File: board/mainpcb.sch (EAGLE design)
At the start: 55 parts, among them IC1 ATMEGA328P, IC2 MAX6921, IC3 7805TV, IC4 DS18B20, J1 2.1MMJACK, Q1 32.768 khz, Q2 IRFD110, SW1 OS102011MA1Q

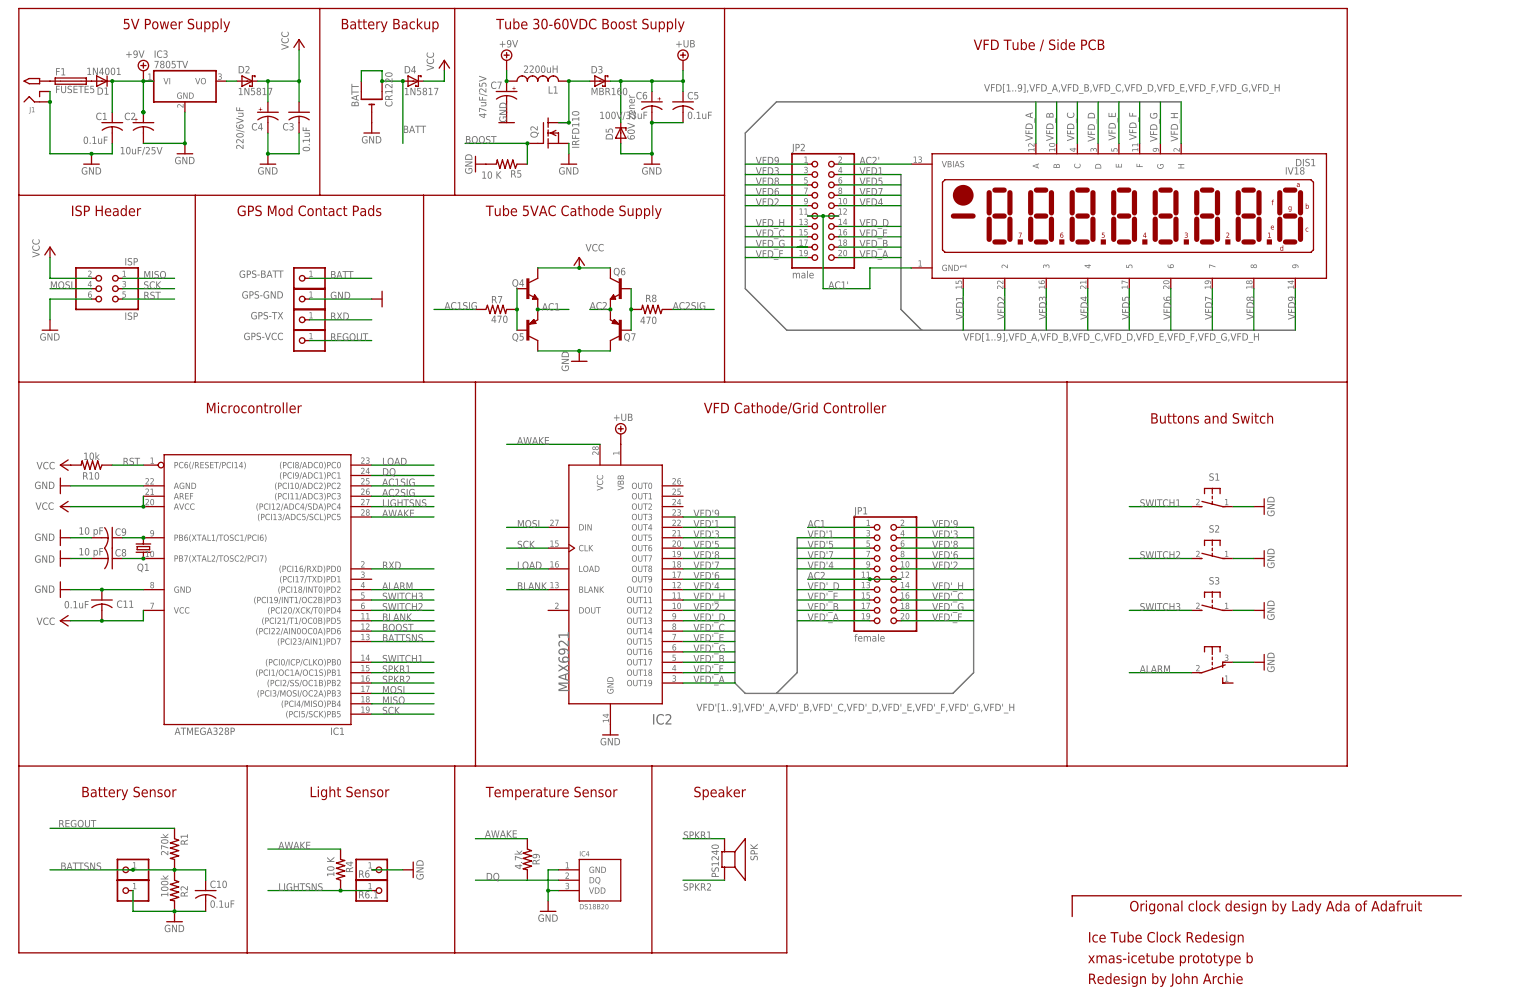
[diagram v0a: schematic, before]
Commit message: Revised the xmas-icetube board
This commit updates the Ice Tube Clock board to revision C.  Although
revision C is untested, the circuit is identical to revision B, so I
cannot imagine that there would be any problems.
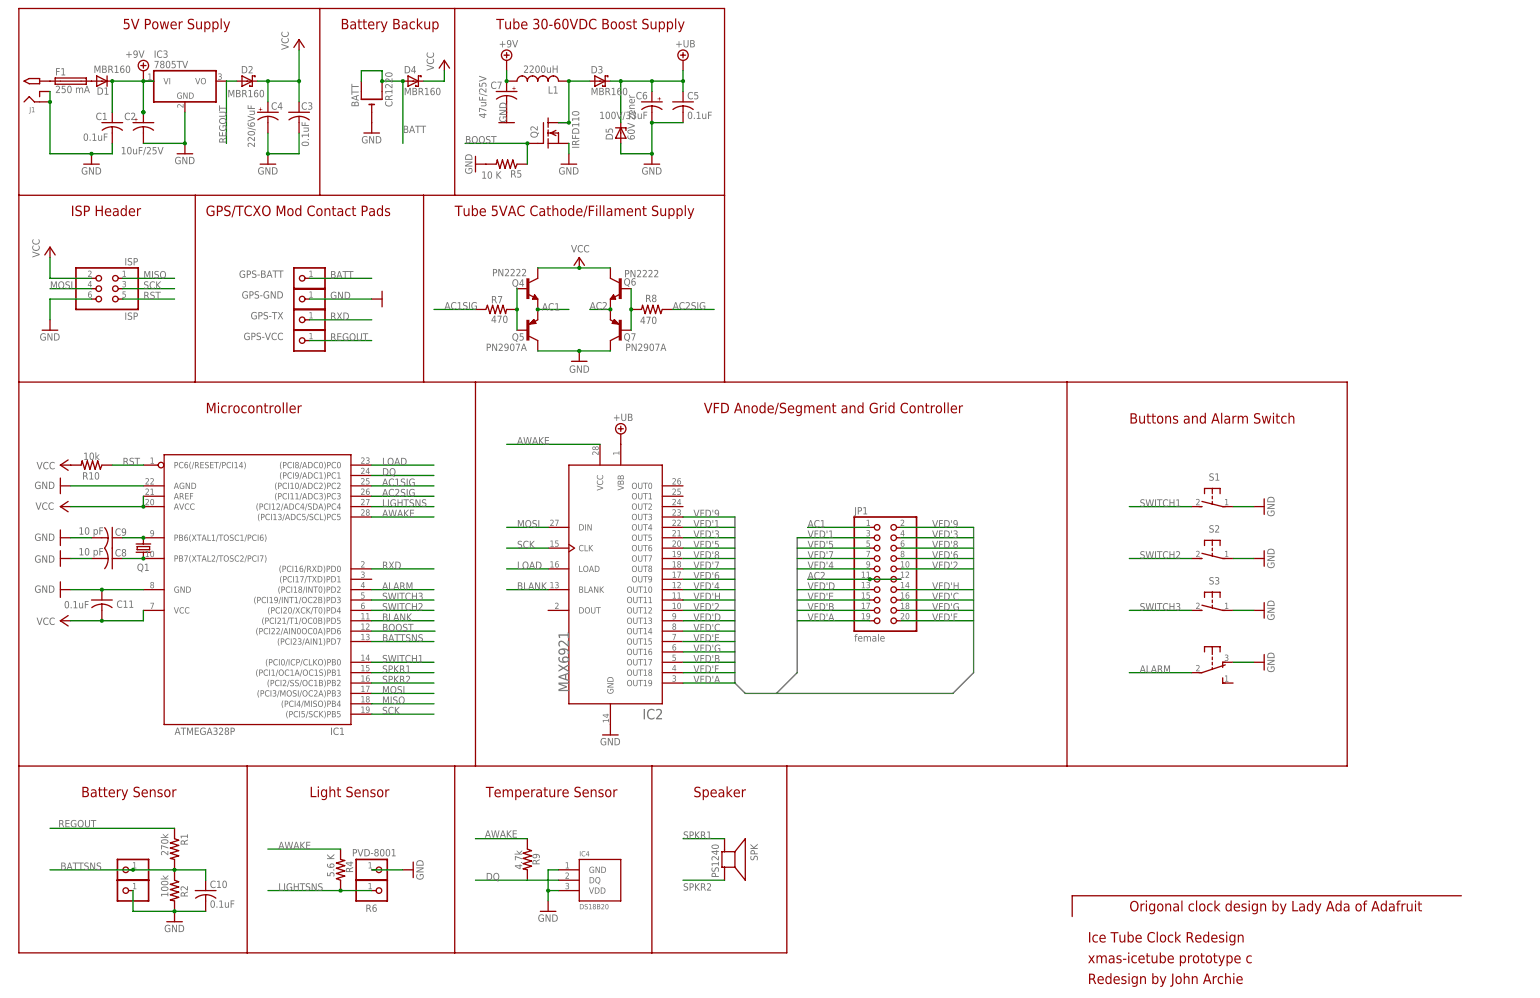
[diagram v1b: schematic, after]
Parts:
- removed DIS1: IV18, vfd:IV18
- removed JP2: male, pinhead:PINHD-2X10
- D1: value 1N4001 -> MBR160
- D2, D4: value 1N5817 -> MBR160
- F1: value FUSETE5 -> 250 mA
- Q4, Q6: value (none) -> PN2222
- Q5, Q7: value (none) -> PN2907A
- R4: value 10 K -> 5.6 K
- R6: value (none) -> PVD-8001
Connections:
- net VFD'_A renamed VFD'A
- net VFD'_B renamed VFD'B
- net VFD'_C renamed VFD'C
- net VFD'_D renamed VFD'D
- net VFD'_E renamed VFD'E
- net VFD'_F renamed VFD'F
- net VFD'_G renamed VFD'G
- net VFD'_H renamed VFD'H
- removed net AC1': DIS1.GND, JP2.11, JP2.12
- removed net AC2': DIS1.VBIAS, JP2.2
- removed net VFD1: DIS1.1, JP2.4
- removed net VFD2: DIS1.2, JP2.9
- removed net VFD3: DIS1.3, JP2.3
- removed net VFD4: DIS1.4, JP2.10
- removed net VFD5: DIS1.5, JP2.6
- removed net VFD6: DIS1.6, JP2.7
- removed net VFD7: DIS1.7, JP2.8
- removed net VFD8: DIS1.8, JP2.5
- removed net VFD9: DIS1.9, JP2.1
- removed net VFD_A: DIS1.A, JP2.20
- removed net VFD_B: DIS1.B, JP2.18
- removed net VFD_C: DIS1.C, JP2.15
- removed net VFD_D: DIS1.D, JP2.14
- removed net VFD_E: DIS1.E, JP2.16
- removed net VFD_F: DIS1.F, JP2.19
- removed net VFD_G: DIS1.G, JP2.17
- removed net VFD_H: DIS1.H, JP2.13
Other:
- note added: "Buttons and Alarm Switch"
- note added: "GPS/TCXO Mod Contact Pads"
- note added: "Tube 5VAC Cathode/Fillament Supply"
- note added: "VFD Anode/Segment and Grid Controller"
- note added: "xmas-icetube prototype c"
- note removed: "Buttons and Switch"
- note removed: "GPS Mod Contact Pads"
- note removed: "Tube 5VAC Cathode Supply"
- note removed: "VFD Cathode/Grid Controller"
- note removed: "VFD Tube / Side PCB"
- note removed: "xmas-icetube prototype b"

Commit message: Revised xmas-icetube board (Rev. D)
The xmas-icetube (Rev D) board is currently *untested*, so use this
design at your own risk.  Rev. D includes an enhancement to the
filament driver circuit to increase filament voltage to within
specifications.  The filament voltage issue has been discussed in the
Adafruit Clocks forum:

  http://forums.adafruit.com/viewtopic.php?p=223798#p223798
  http://forums.adafruit.com/viewtopic.php?p=223793#p223793
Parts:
- added IC5: LM317, jarchie:LM317
- C6: value 100V/33uF -> 33uF
- D1: value MBR160 -> 1N4001
- D2, D4: value MBR160 -> 1N5817
- D5: value 60V zener -> 56V
- IC3: value 7805TV -> 78L05; device linear:7805TV -> jarchie:78L05
- Q4, Q6: value PN2222 -> ZVP2110A; device transistor-neu-to92:-NPN-TO92-EBC -> jarchie:ZVP2110A
- Q5, Q7: value PN2907A -> ZVN2110A; device transistor-neu-to92:-PNP-TO92-EBC -> jarchie:ZVN2110A
- R4: value 5.6 K -> 5.6k
- R5: value 10 K -> 10k
- R7: value 470 -> 1.00k, 1%
- R8: value 470 -> 3.57k, 1%
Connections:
- removed net N$10: Q6.B, Q7.B, R8.2
- removed net N$22: Q4.B, Q5.B, R7.2
- new net N$14: IC5.OUT, Q4.S, Q6.S, R7.1
- new net N$6: IC5.ADJ, R7.2, R8.2
- net +9V: now also IC3.IN, IC5.IN; no longer IC3.VI
- net AC1: now also Q4.D, Q5.D; no longer Q4.E, Q5.E
- net AC1SIG: now also Q4.G, Q5.G; no longer R7.1
- net AC2: now also Q6.D, Q7.D; no longer Q6.E, Q7.E
- net AC2SIG: now also Q6.G, Q7.G; no longer R8.1
- net GND: now also Q5.S, Q7.S, R8.1; no longer Q5.C, Q7.C
- net REGOUT: now also IC3.OUT; no longer IC3.VO
- net VCC: no longer Q4.C, Q6.C
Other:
- note added: "xmas-icetube revision d"
- note removed: "xmas-icetube prototype c"
- moved on the sheet: BATT, C1, C10, C11, C2, C3, C4, C5, C6, C7, C8, C9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

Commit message: Minor change to main board.
I changed the main board schematic slightly and added an
acknowledgements section to the README.
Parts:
- C2: value 10uF/25V -> 47uF
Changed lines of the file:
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@@
 <parts>
 <part name="J1" library="minimidi" deviceset="2.1MMJACK" device=""/>
-<part name="C2" library="minimidi" deviceset="CPOL-US" device="E2.5-6" value="10uF/25V"/>
+<part name="C2" library="minimidi" deviceset="CPOL-US" device="E2.5-6" value="47uF"/>
 <part name="C4" library="minimidi" deviceset="CPOL-US" device="E2.5-6" value="220/6VuF"/>
 <part name="GND5" library="supply1" deviceset="GND" device=""/>
@@
 <instance part="C2" gate="G$1" x="38.1" y="167.64" smashed="yes">
 <attribute name="NAME" x="33.401" y="168.275" size="1.778" layer="95"/>
-<attribute name="VALUE" x="43.053" y="161.671" size="1.778" layer="96" rot="R180"/>
+<attribute name="VALUE" x="37.973" y="164.719" size="1.778" layer="96" rot="R180"/>
 </instance>
 <instance part="C4" gate="G$1" x="68.58" y="170.18" smashed="yes">

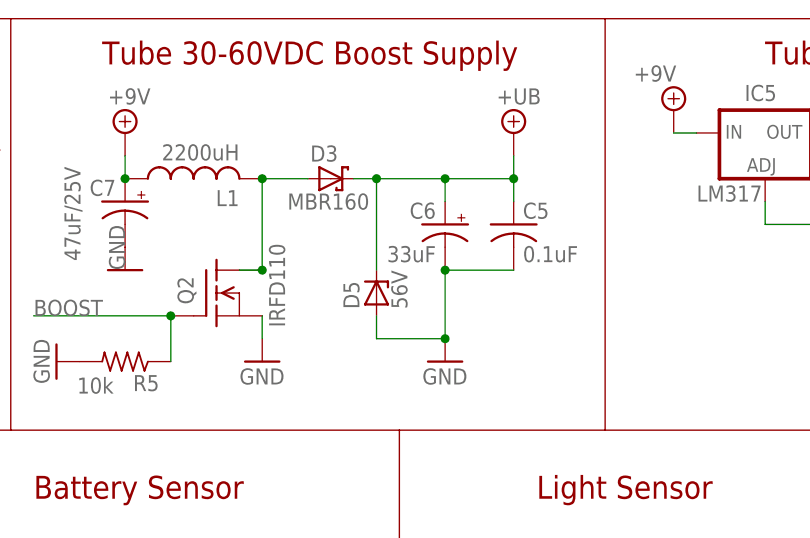
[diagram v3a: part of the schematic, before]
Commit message: Corrected C6 value in board schematic
In both the Ice Tube Clock kit and the xmas-icetube revisions, C6 is
22uF but was marked as 33uF in the schematic.  This has been fixed.
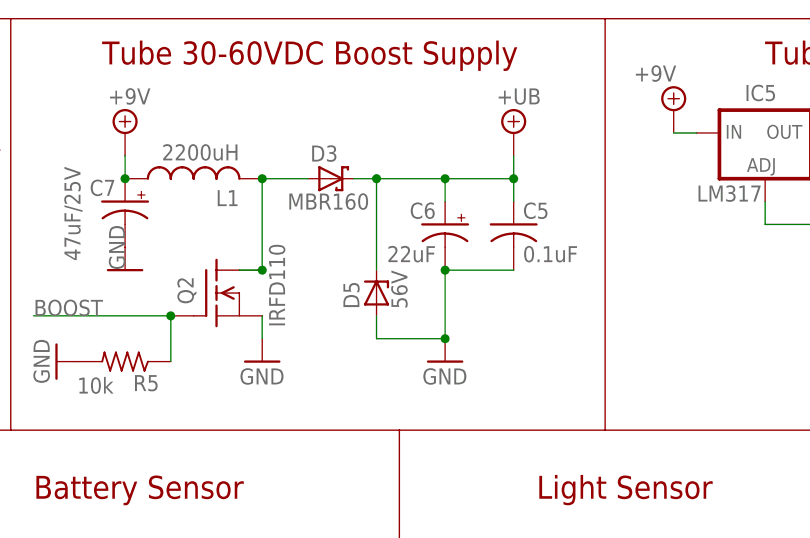
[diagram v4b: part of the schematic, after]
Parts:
- C6: value 33uF -> 22uF
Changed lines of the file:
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@@
 <part name="D3" library="usbbuck" deviceset="SCHOTTKY-DIODE" device="DO41" value="MBR160"/>
 <part name="L1" library="usbbuck" deviceset="L" device="" value="2200uH"/>
-<part name="C6" library="rcl-ez" deviceset="CPOL-US" device="E3.5-8" value="33uF"/>
+<part name="C6" library="rcl-ez" deviceset="CPOL-US" device="E3.5-8" value="22uF"/>
 <part name="V2" library="supply2" deviceset="+9V" device=""/>
 <part name="GND3" library="supply1" deviceset="GND" device=""/>
